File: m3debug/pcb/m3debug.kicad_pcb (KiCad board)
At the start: 2 copper layers, 40 x 49.5 mm, 64 parts, among them IC1 STM32F405RxTx, IC2 MCP2562, IC3 ADP3335, J1 WEST TOP, J2 WEST BOT, J3 EAST TOP, J4 EAST BOT, J5 MICROUSB, J6 CHARGING, J7 PYRO1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

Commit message: gen gerbers
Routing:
- net 5v: track 102.5 -> 92.0 mm
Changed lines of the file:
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@@
     (links 200)
     (no_connects 5)
-    (area 79.924999 80.424999 120.087497 130.075001)
+    (area 79.179762 77.175 120.777381 131.425)
     (thickness 1.6)
     (drawings 28)
-    (tracks 714)
+    (tracks 711)
     (zones 0)
     (modules 64)
@@
   )
   (setup
-    (last_trace_width 0.5)
+    (last_trace_width 0.28)
     (user_trace_width 0.15)
     (user_trace_width 0.2)
@@
     (visible_elements FFFCFF7F)
     (pcbplotparams
-      (layerselection 0x00030_ffffffff)
-      (usegerberextensions false)
+      (layerselection 0x010f0_ffffffff)
+      (usegerberextensions true)
       (excludeedgelayer true)
       (linewidth 0.100000)
@@
       (psnegative false)
       (psa4output false)
-      (plotreference true)
-      (plotvalue true)
+      (plotreference false)
+      (plotvalue false)
       (plotinvisibletext false)
       (padsonsilk false)
@@
       (outputformat 1)
       (mirror false)
-      (drillshape 1)
+      (drillshape 0)
       (scaleselection 1)
-      (outputdirectory ""))
+      (outputdirectory gerbers/))
   )
   (net 0 "")
@@
   (segment (start 101.525 83.725) (end 101.425 83.725) (width 0.5) (layer F.Cu) (net 9))
   (segment (start 101.525 84.675) (end 101.525 83.725) (width 0.28) (layer F.Cu) (net 9))
-  (segment (start 87.8 125.4) (end 82 125.4) (width 0.5) (layer B.Cu) (net 9))
-  (segment (start 90.2 123) (end 87.8 125.4) (width 0.5) (layer B.Cu) (net 9))
-  (segment (start 91.5 123) (end 90.2 123) (width 0.5) (layer B.Cu) (net 9))
   (segment (start 91.5 123) (end 90.9 123) (width 0.5) (layer F.Cu) (net 9))
   (segment (start 101.525 84.675) (end 101.525 86.525) (width 0.28) (layer F.Cu) (net 9))

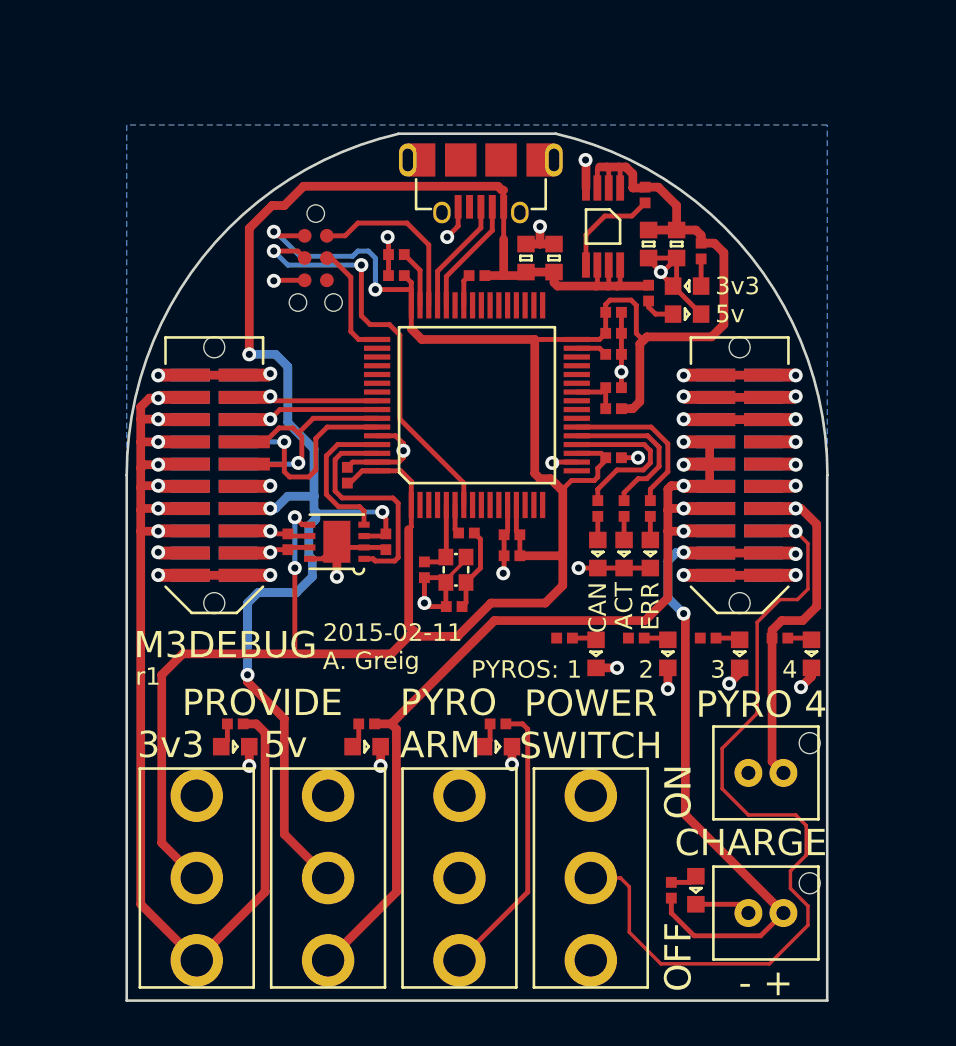
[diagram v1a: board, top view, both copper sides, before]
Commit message: update m3debug to be much more useful
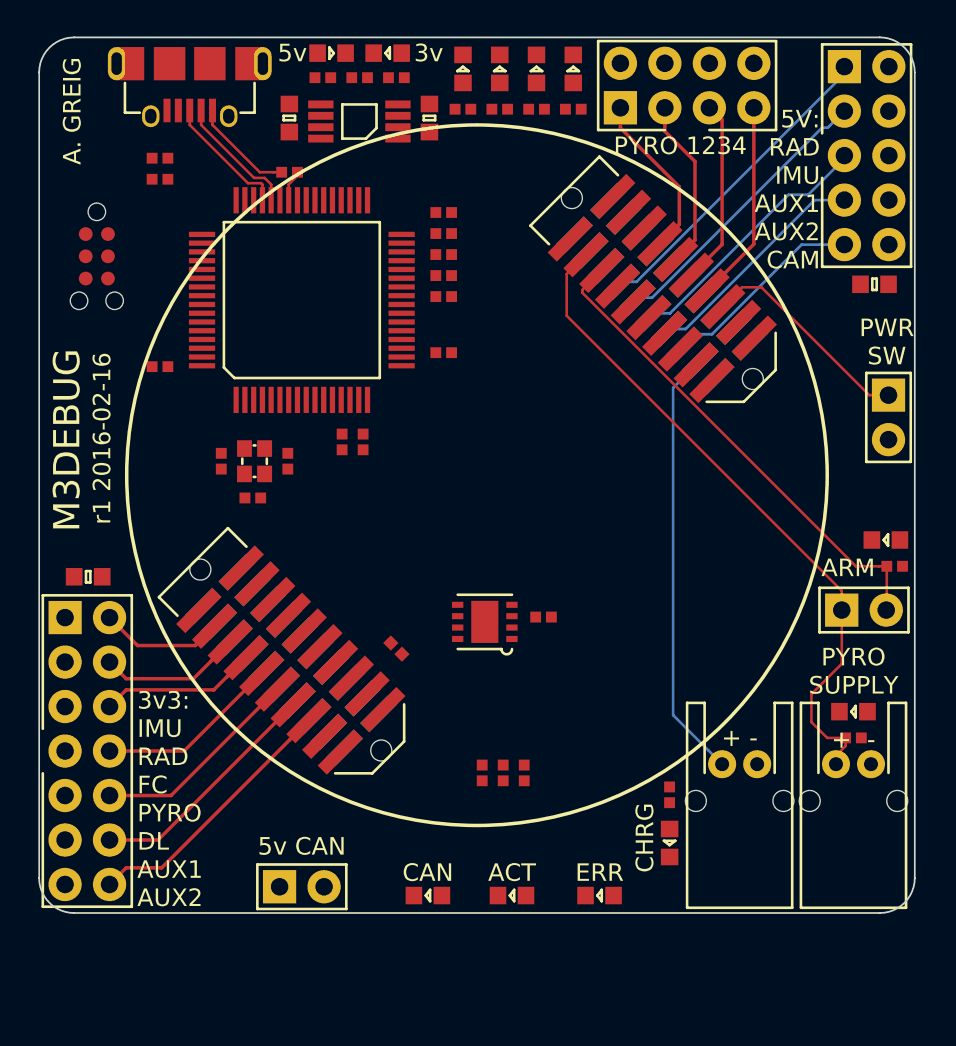
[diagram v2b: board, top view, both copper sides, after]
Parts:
- removed C18: 10µ, agg:0603
- removed D13: RED, agg:0603-LED
- removed R18: 1k, agg:0402
- removed SW1: PYRO_ARMING, agg:A101SYCQ04
- removed SW2: POWER_SWITCH, agg:A101SYCQ04
- removed SW3: SUPPLY_5V, agg:A101SYCQ04
- removed SW4: SUPPLY_3V3, agg:A101SYCQ04
- added C13: 2µ2, agg:0603, F.Cu at (89.3, 79.6)
- added J10: CONN_02x05, agg:DIL-254P-10, F.Cu at (122.2, 81.8)
- added J11: CONN_02x01, agg:SIL-254P-02, F.Cu at (90.0, 123.5)
- added J12: CONN_02x07, agg:DIL-254P-14, F.Cu at (77.8, 115.8)
- added J13: CONN_02x01, agg:SIL-254P-02, F.Cu at (123.5, 96.7)
- added J8: CONN_01x02, agg:S02B-PASK-2, F.Cu at (115.0, 116.5)
- added J9: MICROUSB, agg:MICROUSB_MOLEX_47589-0001, F.Cu at (83.6, 76.5)
- C14: value 10µ -> 1n; footprint agg:0603 -> agg:0402
- C16: value 1n -> 10µ; footprint agg:0402 -> agg:0603
- C17: value 2µ2 -> 10µ
- D1, D2: value GRN -> YLW
- D10, D11: value YLW -> GRN
- D12: value RED -> GRN
- D7, D8: value GRN -> RED
- J5: value MICROUSB -> CONN_01x02; footprint agg:MICROUSB_MOLEX_47589-0001 -> agg:S02B-PASK-2
- J6: value CHARGING -> CONN_02x04; footprint agg:B02B-PASK -> agg:DIL-254P-08
- J7: value PYRO1 -> CONN_02x01; footprint agg:B02B-PASK -> agg:SIL-254P-02
- R2: value 100 -> 1k
- R3: value 4k7 -> 1k
- R4: value 10k -> 1k
- R5: value 120 -> 100
- R6: value 1k -> 120
- R7: value 1k -> 4k7
- R8: value 1k -> 10k
- moved J6 47.5 mm to (112.0, 77.8)
- moved J5 40.5 mm to (121.5, 116.5)
- moved C16 38.6 mm to (77.8, 105.8), turned to 0 degrees
- moved D6 36.9 mm to (103.4, 76.8), turned to 270 degrees
- moved D5 36.1 mm to (101.3, 76.8), turned to 270 degrees
- moved D4 35.4 mm to (99.2, 76.8), turned to 270 degrees
- moved R11 33.2 mm to (103.4, 79.1), turned to 180 degrees
- moved D11 33.1 mm to (91.7, 75.9), turned to 180 degrees
- moved R10 32.5 mm to (101.3, 79.1), turned to 180 degrees
- moved R9 31.8 mm to (99.2, 79.1), turned to 180 degrees
- moved D10 31.0 mm to (94.9, 75.9), turned to 0 degrees
- moved R16 30.0 mm to (91.2, 77.3), turned to 0 degrees
- moved R1 28.4 mm to (100.3, 117.0), turned to 270 degrees
- moved R7 28.2 mm to (98.1, 88.6)
- moved R15 27.2 mm to (95.4, 77.3), turned to 0 degrees
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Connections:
- C12 pad 1: 5v -> /5v_CAN
- C14 pad 1: 5v -> 3v3
- C14 pad 2: GND -> Net-(C14-Pad2)
- C15 pad 1: 5v -> 3v3
- C16 pad 2: Net-(C16-Pad2) -> GND
- C17 pad 1: 3v3 -> 5v
- IC2 pad 3: 5v -> /5v_CAN
- IC3 pad 5: Net-(C16-Pad2) -> Net-(C14-Pad2)
- J1 pad 11: /3v3_AUX1 -> /3v3_DL
- J1 pad 14: 5v -> /5v_CAN
- J1 pad 15: /3v3_AUX1 -> /3v3_AUX2
- J1 pad 3: /3v3_AUX1 -> /3v3_IMU
- J1 pad 5: /3v3_AUX1 -> /3v3_RADIO
- J1 pad 7: /3v3_AUX1 -> /3v3_FC
- J1 pad 9: /3v3_AUX1 -> /3v3_PYRO
- J2 pad 11: /3v3_AUX1 -> /3v3_DL
- J2 pad 14: 5v -> /5v_CAN
- J2 pad 15: /3v3_AUX1 -> /3v3_AUX2
- J2 pad 3: /3v3_AUX1 -> /3v3_IMU
- J2 pad 5: /3v3_AUX1 -> /3v3_RADIO
- J2 pad 7: /3v3_AUX1 -> /3v3_FC
- J2 pad 9: /3v3_AUX1 -> /3v3_PYRO
- J3 pad 13: /5v_AUX1 -> /5v_AUX2
- J3 pad 15: /5v_AUX1 -> /5v_CAM
- J3 pad 7: /5v_AUX1 -> /5v_RADIO
- J3 pad 9: /5v_AUX1 -> /5v_IMU
- J4 pad 13: /5v_AUX1 -> /5v_AUX2
- J4 pad 15: /5v_AUX1 -> /5v_CAM
- J4 pad 7: /5v_AUX1 -> /5v_RADIO
- J4 pad 9: /5v_AUX1 -> /5v_IMU
- J5 pad 1: 5v -> /PYRO_SO
- J5 pad 2: /USB_D- -> GND
- J6 pad 1: /CHARGE -> /PYRO1
- J7 pad 1: /PYRO4 -> /PYRO_SO
- J7 pad 2: GND -> /PYRO_SI
- R1 pad 1: 5v -> /LED0
- R1 pad 2: Net-(IC1-Pad42) -> Net-(D1-Pad2)
- R10 pad 1: /PYRO3 -> /PYRO2
- R11 pad 1: /PYRO4 -> /PYRO3
- R12 pad 1: 5v -> /PYRO4
- R13 pad 1: 3v3 -> /PYRO_SI
- R14 pad 1: /CHARGE -> /PYRO_SO
- R15 pad 1: /LED0 -> 3v3
- R16 pad 1: /LED1 -> 5v
- R17 pad 1: /LED2 -> /CHARGE
- R2 pad 1: Net-(C2-Pad1) -> /LED1
- R2 pad 2: Net-(IC1-Pad6) -> Net-(D2-Pad2)
- R3 pad 1: 3v3 -> /LED2
- R3 pad 2: /TPWR_MON -> Net-(D3-Pad2)
- R4 pad 1: /TPWR_MON -> 5v
- R4 pad 2: GND -> Net-(IC1-Pad42)
- R5 pad 1: /CAN+ -> Net-(C2-Pad1)
- R5 pad 2: /CAN- -> Net-(IC1-Pad6)
- R6 pad 1: /5v_AUX1 -> /CAN+
- R6 pad 2: Net-(D1-Pad2) -> /CAN-
- R7 pad 1: /3v3_AUX1 -> 3v3
- R7 pad 2: Net-(D2-Pad2) -> /TPWR_MON
- R8 pad 1: /PYRO1 -> /TPWR_MON
- R8 pad 2: Net-(D3-Pad2) -> GND
- R9 pad 1: /PYRO2 -> /PYRO1
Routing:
- net 3v3: track 149.0 -> 0.00 mm, vias 4 -> 0
- net GND: track 117.2 -> 0.00 mm, vias 29 -> 0
- net 5v: track 92.0 -> 5.89 mm, vias 4 -> 0
- net /3v3_AUX1: track 79.8 -> 13.7 mm, vias 7 -> 0
- net /5v_AUX1: track 63.2 -> 14.7 mm, vias 5 -> 0
- net /PWR: track 50.1 -> 12.5 mm, vias 1 -> 0
- net /PYRO_SO: track 12.9 -> 38.4 mm, vias 2 -> 0
- net /~RST: track 24.0 -> 0.00 mm, vias 2 -> 0
- net /CHARGE: track 45.2 -> 24.9 mm, vias 3 -> 0
- net /5v_RADIO: track 0.00 -> 18.0 mm
- net /5v_IMU: track 0.00 -> 16.2 mm
- net /3v3_AUX2: track 0.00 -> 15.3 mm
- net /JTDO: track 14.3 -> 0.00 mm, vias 1 -> 0
- net /JTDI: track 13.7 -> 0.00 mm, vias 1 -> 0
- net /CAN_TXD: track 13.4 -> 0.00 mm
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- removed copper zone on B.Cu, net GND
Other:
- board size 40 x 49.5 mm -> 50 x 50 mm
- net class Default: trace_width 0.28 -> 0.2
- rule via_min_drill: 0.3 -> 0.4
- rule via_min_size: 0.6 -> 0.8
- board text added: "+ -"
- board text added: "3v"
- board text added: "3v3: IMU RAD FC PYRO DL AUX1 AUX2"
- board text added: "5V: RAD IMU AUX1 AUX2 CAM"
- board text added: "5v CAN"
- board text added: "A. GREIG"
- board text added: "ARM"
- board text added: "CHRG"
- board text added: "PWR SW"
- board text added: "PYRO 1234"
- board text added: "PYRO SUPPLY"
- board text added: "r1 2016-02-16"
- board text removed: "- +"
- board text removed: "2"
- board text removed: "2015-02-11 A. Greig"
- board text removed: "3"
- board text removed: "3v3"
- board text removed: "4"
- board text removed: "CHARGE"
- board text removed: "OFF"
- board text removed: "ON"
- board text removed: "POWER SWITCH"
- board text removed: "PROVIDE"
- board text removed: "PYRO 4"
- board text removed: "PYRO ARM"
- board text removed: "PYROS: 1"
- board text removed: "r1"

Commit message: route a lot of m3debug
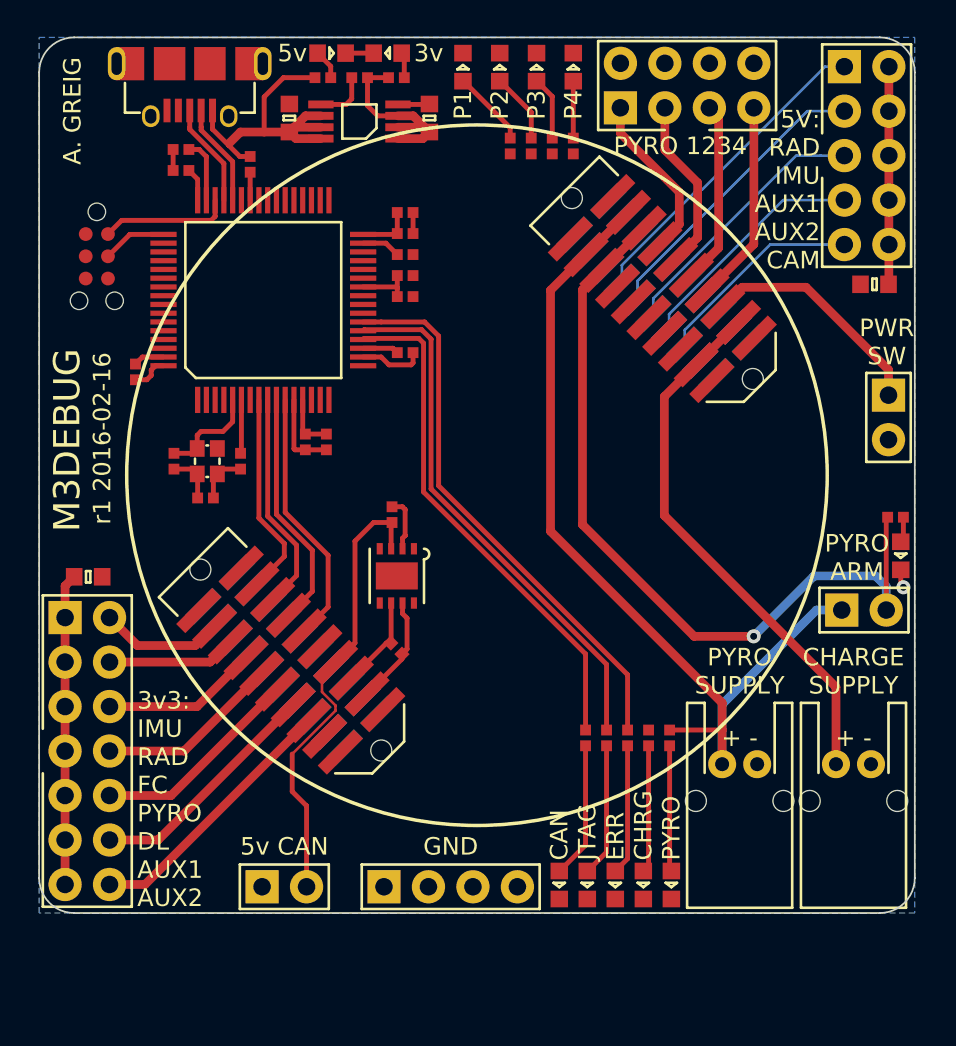
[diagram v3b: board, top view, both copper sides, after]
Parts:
- added J14: GND, agg:SIL-254P-04, F.Cu at (98.5, 123.5)
- J10: value CONN_02x05 -> 5V_SUPPLY
- J11: value CONN_02x01 -> CAN_SUPPLY
- J12: value CONN_02x07 -> 3V3_SUPPLY
- J13: value CONN_02x01 -> PWRSW
- J5: value CONN_01x02 -> PYRO_SUPPLY
- J6: value CONN_02x04 -> PYROS
- J7: value CONN_02x01 -> PYRO_ARM
- J8: value CONN_01x02 -> CHARGE
- moved D9 14.4 mm to (111.1, 123.4), turned to 90 degrees
- moved R14 10.5 mm to (111.0, 115.0), turned to 270 degrees
- moved C12 10.4 mm to (95.2, 102.2), turned to 90 degrees
- moved D1 7.52 mm to (104.7, 123.4), turned to 90 degrees
- moved J5 6.50 mm to (115.0, 116.5)
- moved J8 6.50 mm to (121.5, 116.5)
- moved R1 6.23 mm to (106.2, 115.0)
- moved R2 6.23 mm to (107.4, 115.0), turned to 270 degrees
- moved R3 6.23 mm to (108.6, 115.0)
- moved IC2 5.67 mm to (95.4, 105.8), turned to 270 degrees
- moved D2 4.34 mm to (106.3, 123.4), turned to 90 degrees
- moved R17 3.46 mm to (109.8, 115.0)
- moved R9 3.42 mm to (101.9, 81.2), turned to 90 degrees
- moved D12 2.83 mm to (109.5, 123.4)
- moved R13 2.80 mm to (123.9, 102.4)
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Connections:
- IC1 pad 10: (no net) -> /JTDI
- IC1 pad 11: (no net) -> /JTDO
- IC1 pad 56: /JTMS -> (no net)
- IC1 pad 57: /JTCK -> (no net)
- IC1 pad 58: /JTDI -> (no net)
- IC1 pad 59: /JTDO -> (no net)
- IC1 pad 8: (no net) -> /JTMS
- IC1 pad 9: (no net) -> /JTCK
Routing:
- net 3v3: track 0.00 -> 41.1 mm
- net /LED2: track 0.00 -> 31.6 mm
- net /LED1: track 0.00 -> 30.6 mm
- net /LED0: track 0.00 -> 29.5 mm
- net /5v_CAN: track 0.00 -> 26.3 mm
- net 5v: track 5.89 -> 31.5 mm
- net GND: track 0.00 -> 22.9 mm, vias 0 -> 1
- net /PYRO_SI: track 28.1 -> 46.7 mm, vias 0 -> 1
- net /JTDO: track 0.00 -> 14.8 mm
- net /PYRO_SO: track 38.4 -> 52.9 mm
- net /JTDI: track 0.00 -> 13.7 mm
- net /JTCK: track 0.00 -> 12.6 mm
- net /JTMS: track 0.00 -> 11.7 mm
- net Net-(D1-Pad2): track 0.00 -> 7.79 mm
- net Net-(D2-Pad2): track 0.00 -> 7.62 mm
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- added copper zone on B.Cu, net GND
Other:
- board text added: "CHARGE SUPPLY"
- board text added: "GND"
- board text added: "JTAG"
- board text added: "P1"
- board text added: "P2"
- board text added: "P3"
- board text added: "P4"
- board text added: "PYRO"
- board text added: "PYRO ARM"
- board text removed: "ACT"
- board text removed: "ARM"

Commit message: ripup and restart routing
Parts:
- moved D12 1.60 mm to (111.1, 123.4)
- moved D9 1.60 mm to (109.5, 123.4)
- moved R14 1.20 mm to (109.8, 115.0)
- moved R17 1.20 mm to (111.0, 115.0)
- moved C2 0.32 mm to (84.2, 101.4)
- moved C1 0.32 mm to (82.4, 99.3)
- moved R5 0.32 mm to (86.2, 99.3)
- moved Y1 0.32 mm to (84.3, 99.3)
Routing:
- net /PYRO_SI: track 46.7 -> 0.00 mm, vias 1 -> 0
- net /PYRO_SO: track 52.9 -> 6.37 mm
- net GND: track 22.9 -> 61.2 mm, vias 1 -> 8
- net /LED2: track 31.6 -> 0.00 mm
- net /LED1: track 30.6 -> 0.00 mm
- net /LED0: track 29.5 -> 0.00 mm
- net /5v_CAN: track 26.3 -> 5.78 mm, vias 0 -> 1
- net /5v_RADIO: track 18.4 -> 0.00 mm
- net /5v_IMU: track 16.8 -> 0.00 mm
- net /CHARGE: track 31.0 -> 15.4 mm
- net /5v_AUX1: track 15.1 -> 0.00 mm
- net /JTDO: track 14.8 -> 0.00 mm
- net /JTDI: track 13.7 -> 0.00 mm
- net /5v_AUX2: track 13.6 -> 0.00 mm
- net /PWR: track 13.3 -> 0.00 mm
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
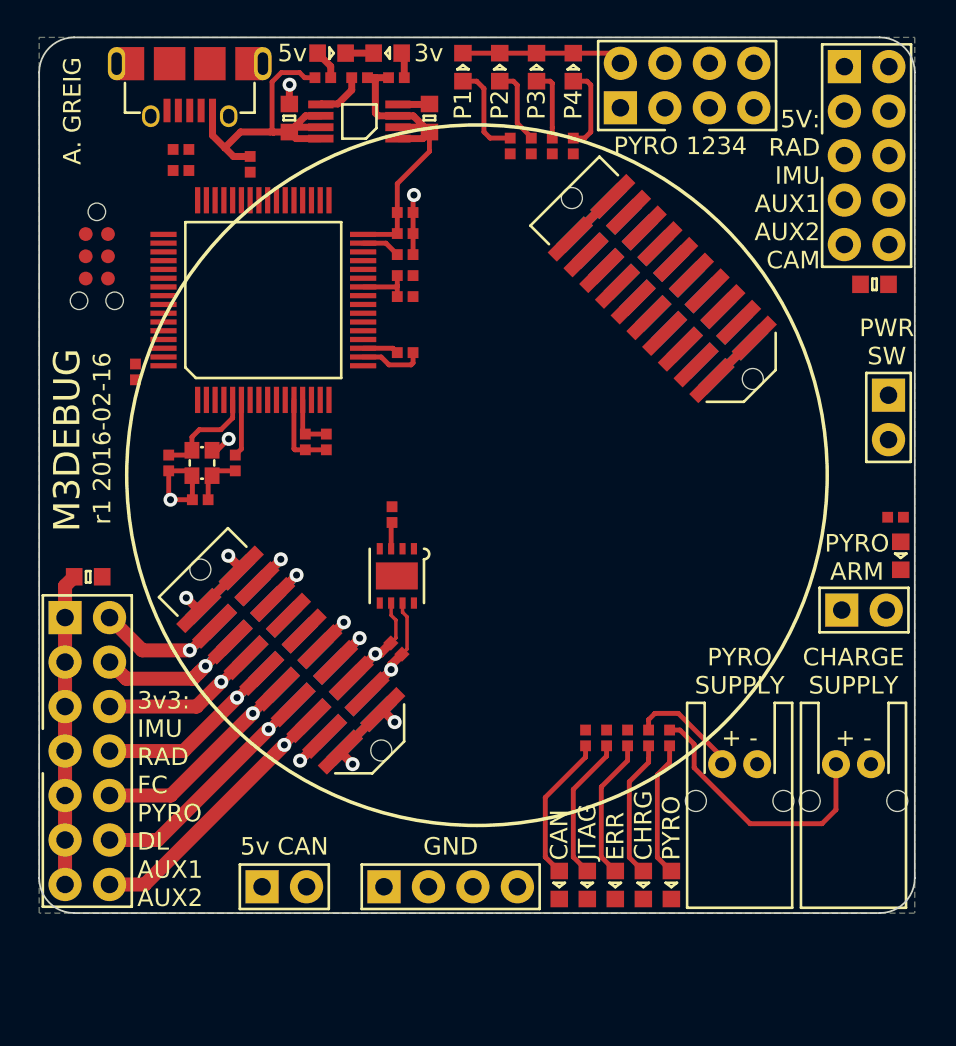
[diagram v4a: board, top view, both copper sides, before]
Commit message: Update m3debug routing
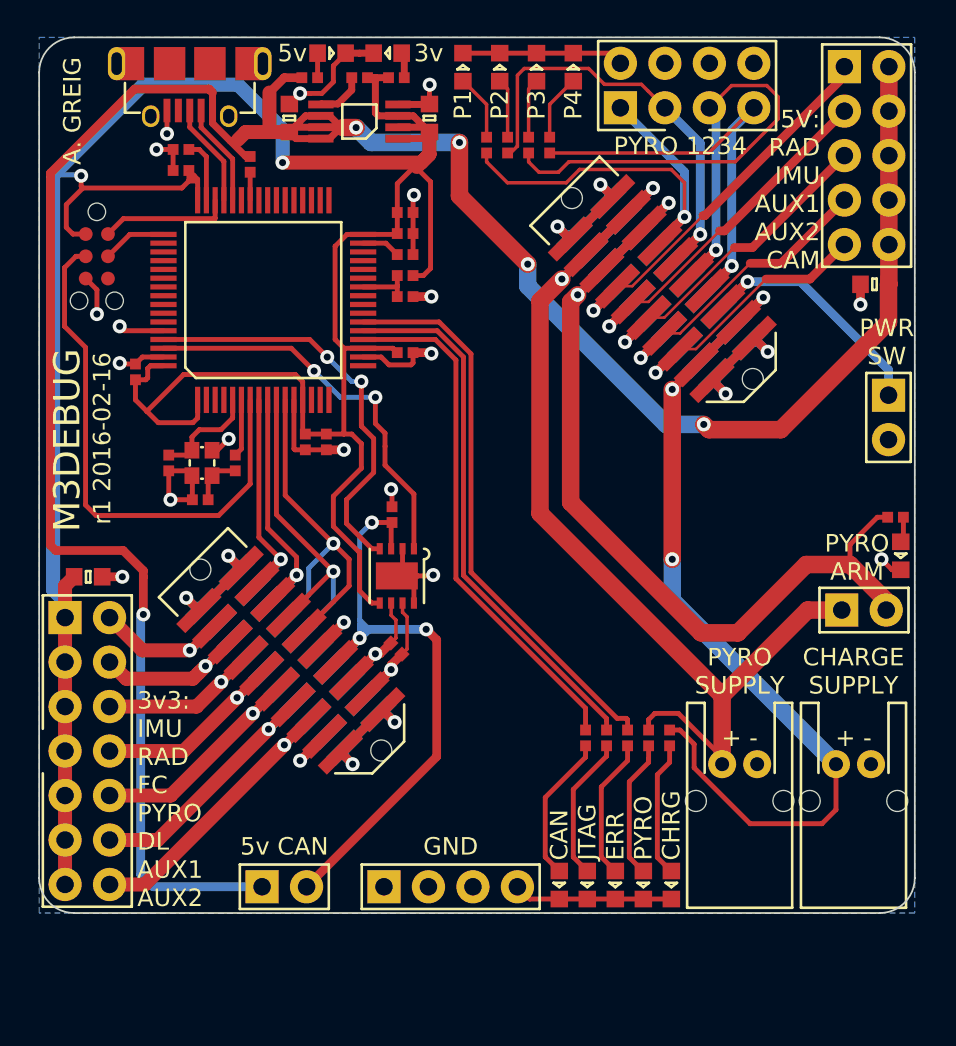
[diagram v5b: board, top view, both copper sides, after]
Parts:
- moved R9 1.35 mm to (100.5, 81.2)
- moved R10 1.35 mm to (101.8, 81.2)
- moved R11 1.35 mm to (103.0, 81.2)
- moved R12 1.35 mm to (104.2, 81.2)
- moved R16 0.75 mm to (90.5, 77.3)
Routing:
- net 3v3: track 42.2 -> 167.0 mm, vias 0 -> 2
- net 5v: track 19.9 -> 144.3 mm, vias 0 -> 5
- net /PYRO_SO: track 6.37 -> 62.5 mm, vias 0 -> 2
- net /PYRO_SI: track 0.00 -> 54.9 mm, vias 0 -> 2
- net GND: track 61.2 -> 113.1 mm, vias 8 -> 26
- net /CHARGE: track 15.4 -> 55.5 mm, vias 0 -> 3
- net /PYRO3: track 0.00 -> 34.9 mm, vias 0 -> 1
- net /LED2: track 0.00 -> 32.4 mm
- net /5v_CAN: track 5.78 -> 37.7 mm, vias 1 -> 3
- net /LED1: track 0.00 -> 31.0 mm
- net /~RST: track 0.00 -> 30.7 mm
- net /LED0: track 0.00 -> 30.0 mm
- net /PYRO1: track 0.00 -> 27.3 mm, vias 0 -> 1
- net /PYRO2: track 0.00 -> 26.7 mm, vias 0 -> 1
- net /PYRO4: track 0.00 -> 26.6 mm, vias 0 -> 1
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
